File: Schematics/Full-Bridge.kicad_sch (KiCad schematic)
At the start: 0 parts

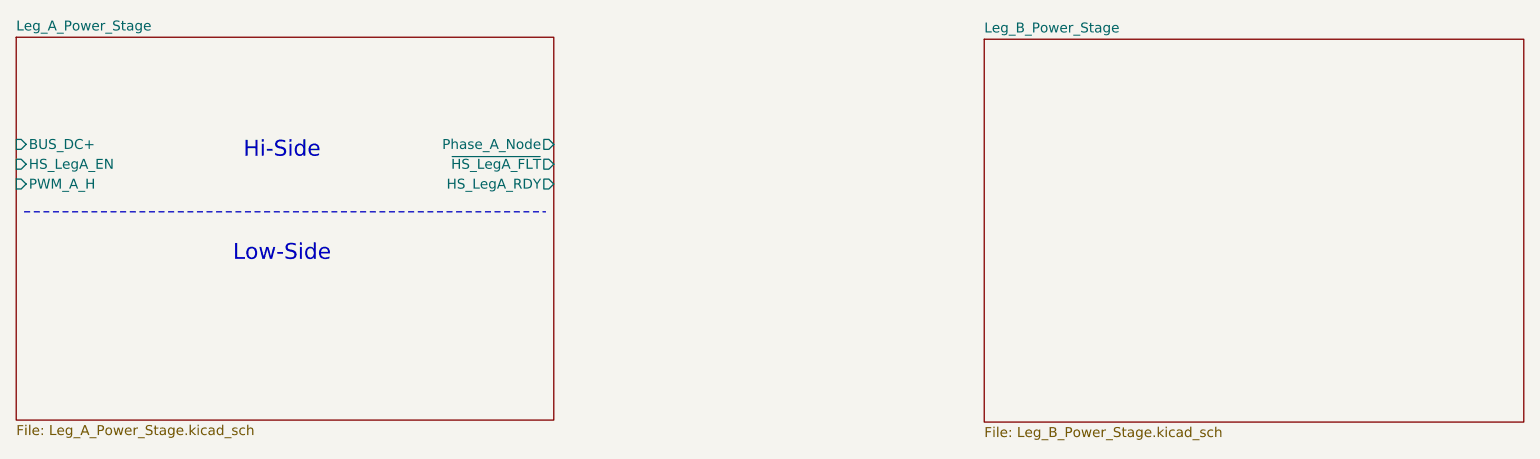
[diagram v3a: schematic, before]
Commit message: Adding 100 pf caps to Leg A circuit, WIP texts
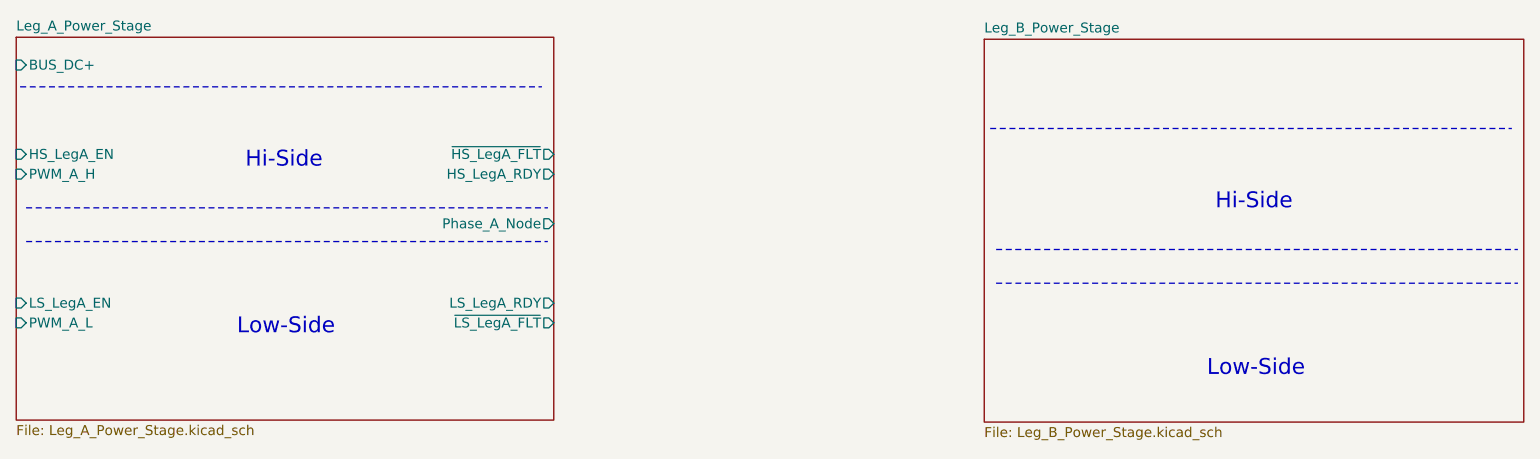
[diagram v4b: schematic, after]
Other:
- sheet Leg_A_Power_Stage ports: added LS_LegA_EN, LS_LegA_RDY, PWM_A_L, ~{LS_LegA_FLT}; removed none
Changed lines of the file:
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@@
 	(generator_version "9.0")
 	(paper "A4")
+	(text "Hi-Side\n"
+		(exclude_from_sim no)
+		(at 214.122 98.806 0)
+		(effects
+			(font
+				(size 2.032 2.032)
+			)
+		)
+	)
 	(text "Low-Side\n"
 		(exclude_from_sim no)
-		(at 89.662 105.41 0)
+		(at 90.17 114.808 0)
+		(effects
+			(font
+				(size 2.032 2.032)
+			)
+		)
+	)
+	(text "Low-Side\n"
+		(exclude_from_sim no)
+		(at 214.376 120.142 0)
 		(effects
 			(font
@@
 	(text "Hi-Side\n"
 		(exclude_from_sim no)
-		(at 89.662 92.202 0)
-		(effects
-			(font
-				(size 2.032 2.032)
-			)
-		)
-	)
-	(polyline
-		(pts
-			(xy 56.642 100.076) (xy 123.444 100.076)
+		(at 89.916 93.472 0)
+		(effects
+			(font
+				(size 2.032 2.032)
+			)
+		)
+	)
+	(polyline
+		(pts
+			(xy 181.102 104.902) (xy 247.904 104.902)
+		)
+		(stroke
+			(width 0)
+			(type dash)
+		)
+	)
+	(polyline
+		(pts
+			(xy 180.34 89.408) (xy 247.142 89.408)
+		)
+		(stroke
+			(width 0)
+			(type dash)
+		)
+	)
+	(polyline
+		(pts
+			(xy 56.896 103.886) (xy 123.698 103.886)
+		)
+		(stroke
+			(width 0)
+			(type dash)
+		)
+	)
+	(polyline
+		(pts
+			(xy 56.896 99.568) (xy 123.698 99.568)
+		)
+		(stroke
+			(width 0)
+			(type dash)
+		)
+	)
+	(polyline
+		(pts
+			(xy 56.134 84.074) (xy 122.936 84.074)
+		)
+		(stroke
+			(width 0)
+			(type dash)
+		)
+	)
+	(polyline
+		(pts
+			(xy 181.102 109.22) (xy 247.904 109.22)
 		)
 		(stroke
@@
 		)
 		(pin "BUS_DC+" input
-			(at 55.626 91.44 180)
+			(at 55.626 81.28 180)
 			(effects
 				(font
@@
 		)
 		(pin "HS_LegA_EN" input
-			(at 55.626 93.98 180)
+			(at 55.626 92.71 180)
 			(effects
 				(font
@@
 		)
 		(pin "HS_LegA_RDY" output
-			(at 124.46 96.52 0)
+			(at 124.46 95.25 0)
 			(effects
 				(font
@@
 		)
 		(pin "Phase_A_Node" output
-			(at 124.46 91.44 0)
+			(at 124.46 101.6 0)
 			(effects
 				(font
@@
 		)
 		(pin "PWM_A_H" input
-			(at 55.626 96.52 180)
+			(at 55.626 95.25 180)
 			(effects
 				(font
@@
 		)
 		(pin "~{HS_LegA_FLT}" output
-			(at 124.46 93.98 0)
-			(effects
-				(font
+			(at 124.46 92.71 0)
+			(effects
+				(font
+					(size 1.27 1.27)
+				)
+				(justify right)
+			)
+		)
+		(pin "LS_LegA_EN" input
+			(at 55.626 111.76 180)
+			(effects
+				(font
+					(size 1.27 1.27)
+				)
+				(justify left)
+			)
+		)
+		(pin "LS_LegA_RDY" output
+			(at 124.46 111.76 0)
+			(effects
+				(font
+					(size 1.27 1.27)
+				)
+				(justify right)
+			)
+		)
+		(pin "PWM_A_L" input
+			(at 55.626 114.3 180)
+			(effects
+				(font
+					(size 1.27 1.27)
+				)
+				(justify left)
+			)
+		)
+		(pin "~{LS_LegA_FLT}" output
+			(at 124.46 114.3 0)
+			(effects
+				(font

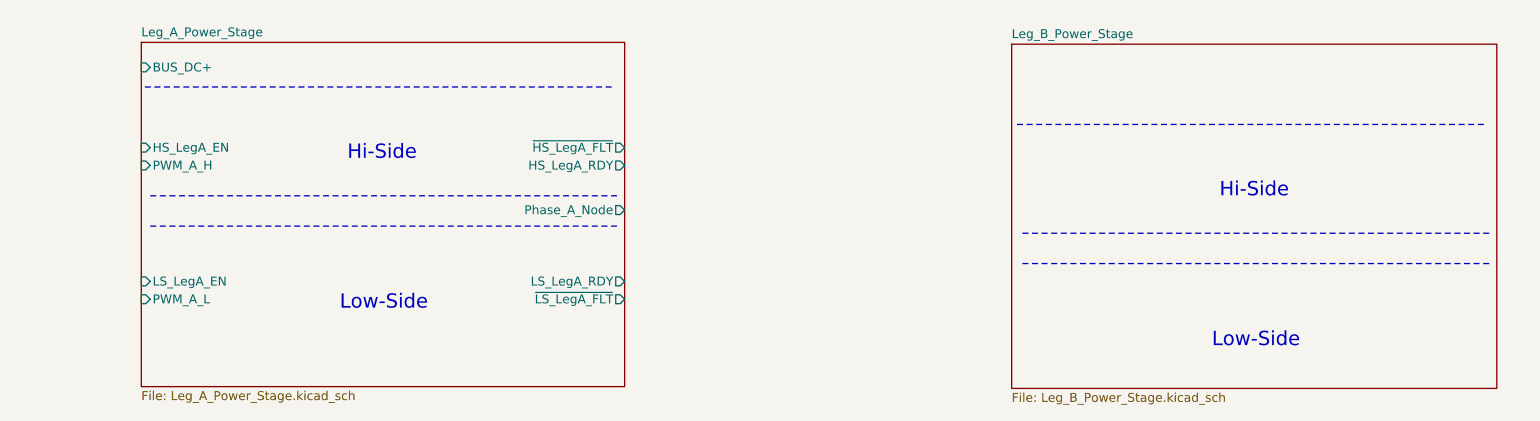
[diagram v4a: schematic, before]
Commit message: [WIP Full Bridge]
- Finished Leg B and cleaned up sub sheets Leg A and Leg B
- Added Hierarchical sheet pins for Leg A,B and Full Bridge
- Added power schamtic for future use
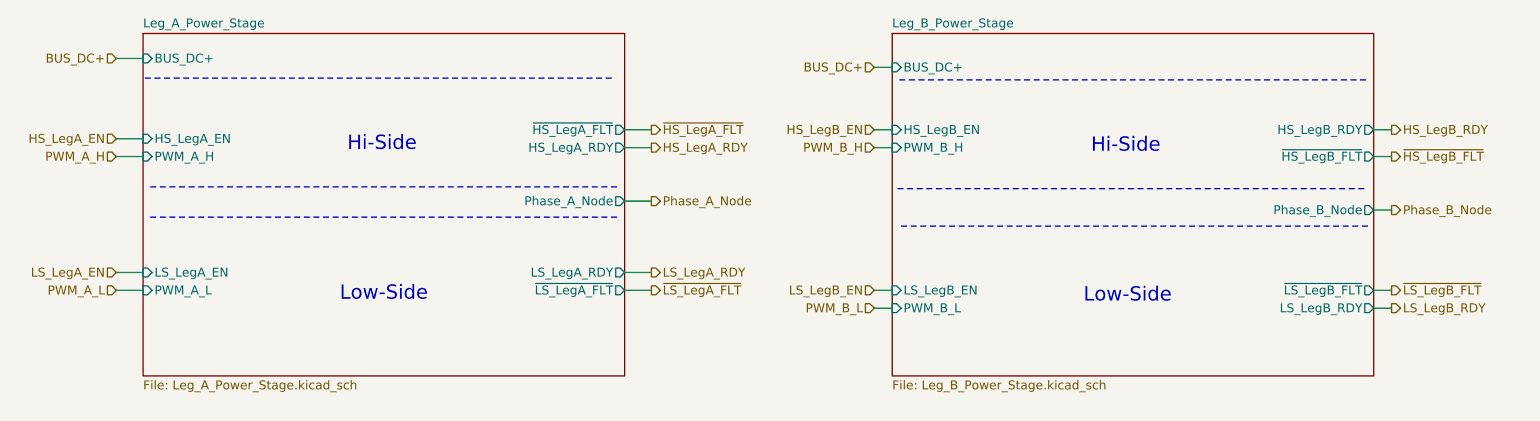
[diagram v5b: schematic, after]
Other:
- sheet Leg_B_Power_Stage ports: added BUS_DC+, HS_LegB_EN, HS_LegB_RDY, LS_LegB_EN, LS_LegB_RDY, PWM_B_H, PWM_B_L, Phase_B_Node, ~{HS_LegB_FLT}, ~{LS_LegB_FLT}; removed none

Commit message: Changing Text to Text Block
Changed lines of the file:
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@@
+		)
+	)
+	(text_box "Leg_B_Power_Stage"
+		(exclude_from_sim no)
+		(at 162.56 73.152 0)
+		(size 20.32 3.048)
+		(margins 0.9525 0.9525 0.9525 0.9525)
+		(stroke
+			(width 0)
+			(type solid)
+		)
+		(fill
+			(type color)
+			(color 0 0 255 0.1)
+		)
+		(effects
+			(font
+				(size 1.27 1.27)
+			)
+			(justify left top)
+		)
+	)
+	(text_box "Leg_A_Power_Stage"
+		(exclude_from_sim no)
+		(at 55.88 73.152 0)
+		(size 20.32 3.048)
+		(margins 0.9525 0.9525 0.9525 0.9525)
+		(stroke
+			(width 0)
+			(type solid)
+		)
+		(fill
+			(type color)
+			(color 0 0 255 0.1)
+		)
+		(effects
+			(font
+				(size 1.27 1.27)
+			)
+			(justify left top)
 		)
 	)
@@
 				)
 				(justify left bottom)
+				(hide yes)
 			)
 		)
@@
 				)
 				(justify left bottom)
-			)
-		)
+				(hide yes)
+			)
+		)

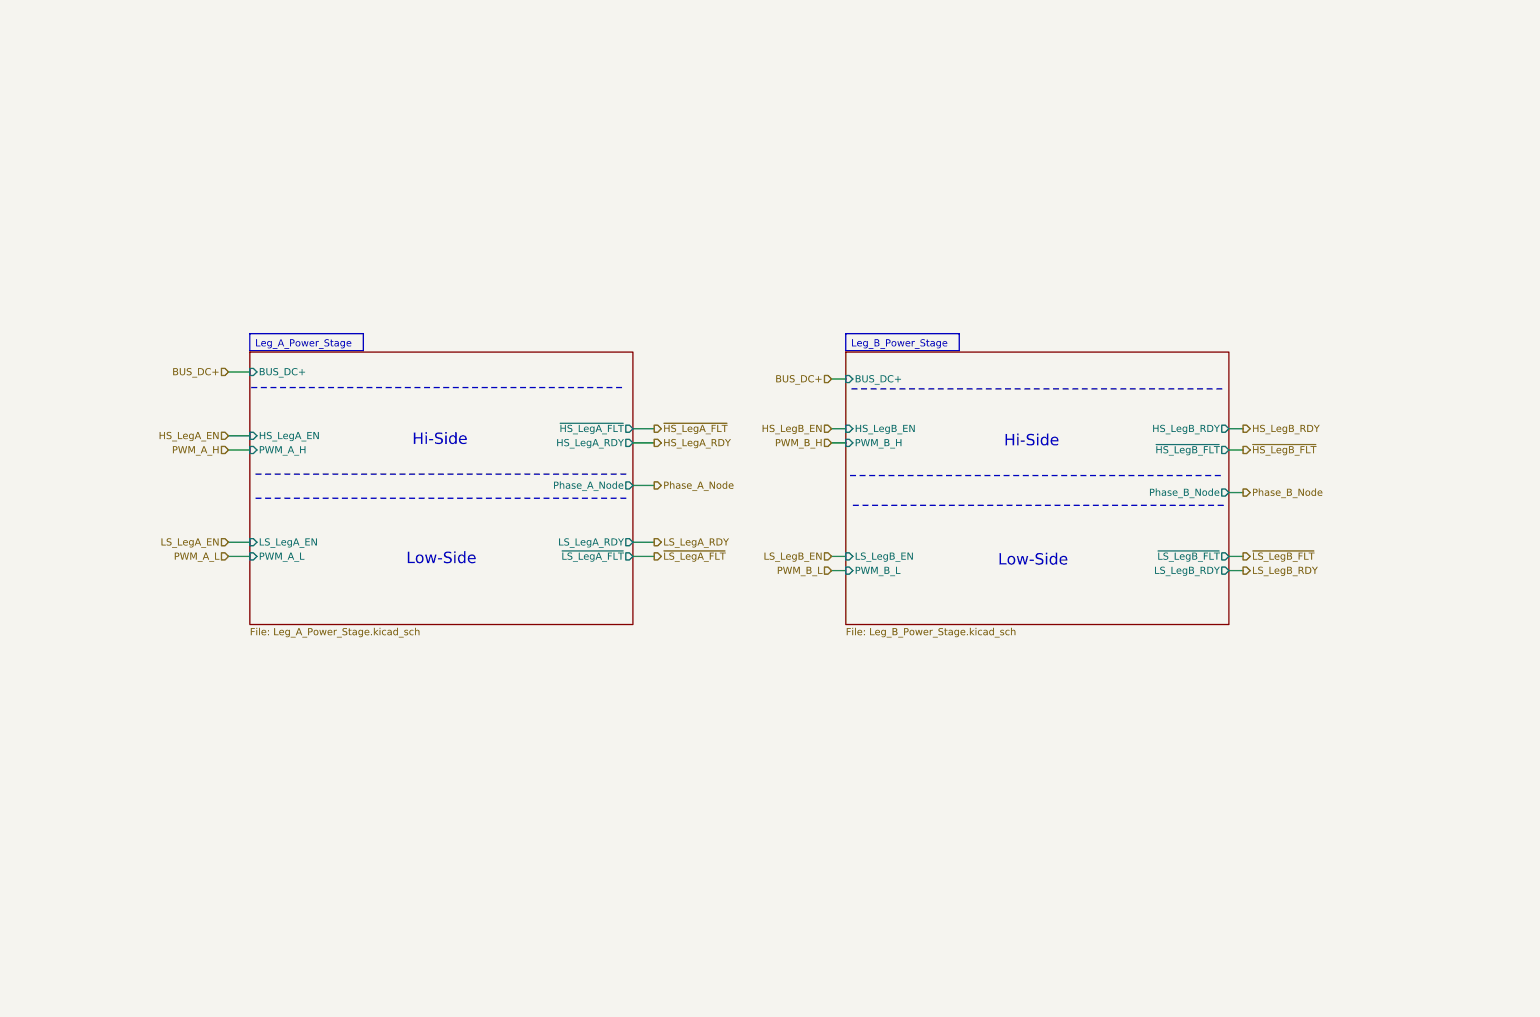
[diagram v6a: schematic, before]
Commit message: [WIP Single Phase SiC Inverter]
- Added molex 4 pin pcb connector for +15V power
- Added 3d model, symbol and footprint
- Added datasheet for molex connector
- Added Male and Female pcb - pcb connectors to all sub sheets
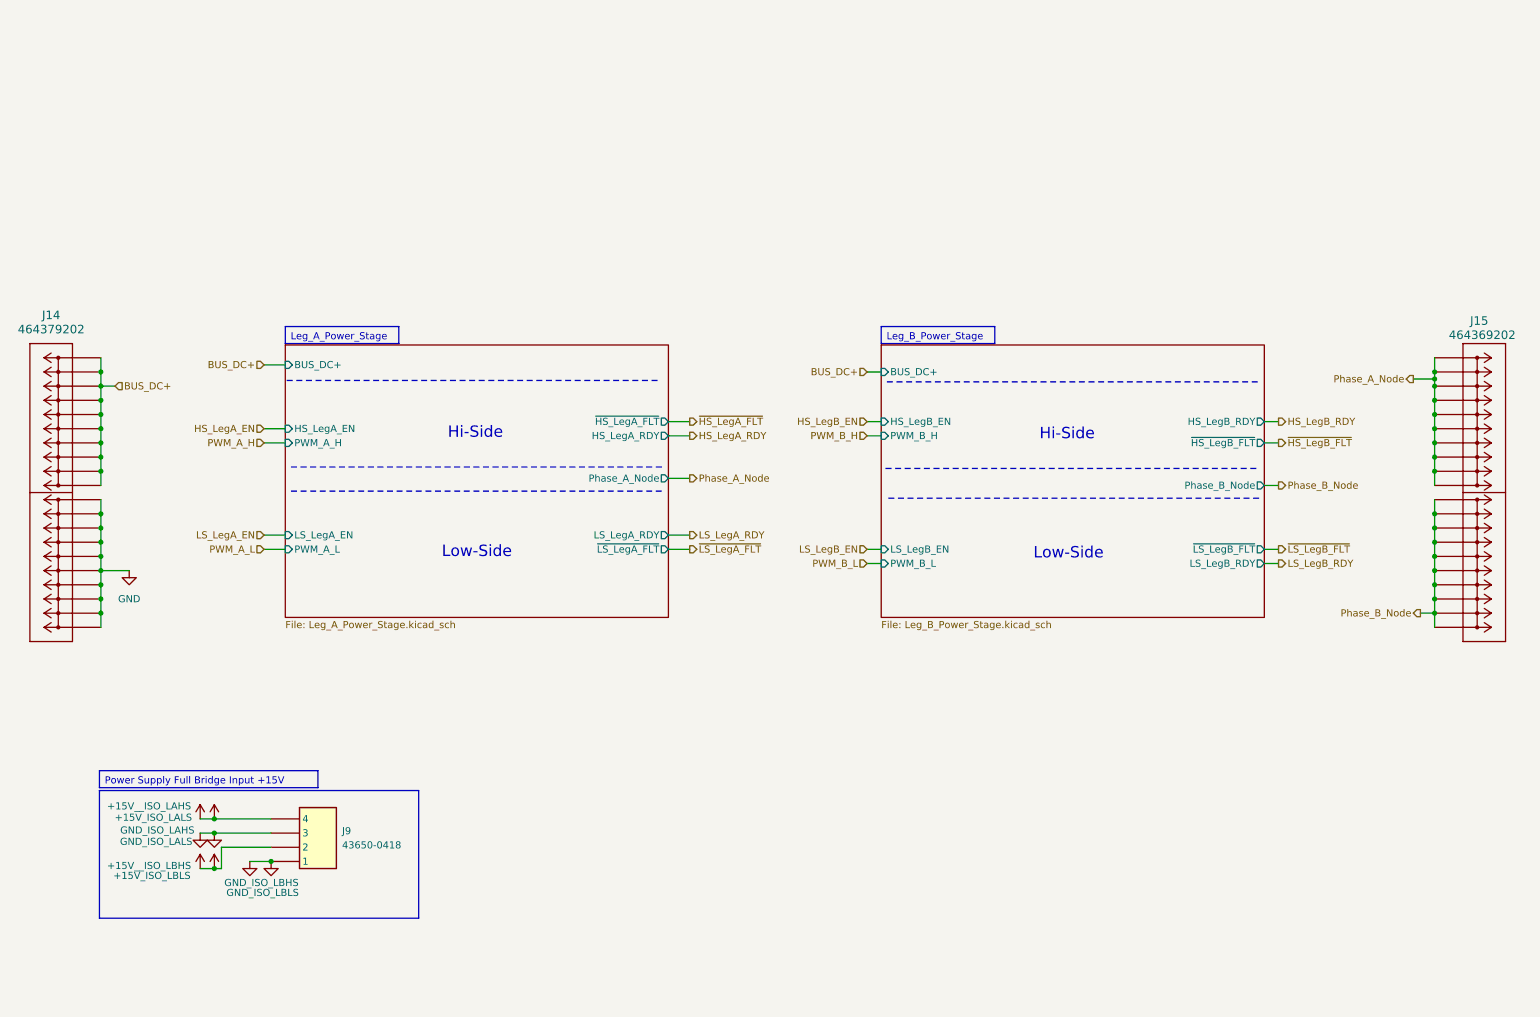
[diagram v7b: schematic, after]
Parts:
- added J14: 464379202, SiC_Inverter:46437-900_02, symbol SiC_Inverter:464379202
- added J15: 464369202, SiC_Inverter:46436-900_02, symbol SiC_Inverter:464369202
- added J9: 43650-0418, SiC_Inverter:436500418, symbol SiC_Inverter:43650-0418
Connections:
- net BUS_DC+: now also J14.P2_1, J14.P2_10, J14.P2_2, J14.P2_3, J14.P2_4, J14.P2_5, J14.P2_6, J14.P2_7, J14.P2_8, J14.P2_9
- net Phase_A_Node: now also J15.P1_1, J15.P1_10, J15.P1_2, J15.P1_3, J15.P1_4, J15.P1_5, J15.P1_6, J15.P1_7, J15.P1_8, J15.P1_9
- net Phase_B_Node: now also J15.P2_1, J15.P2_10, J15.P2_2, J15.P2_3, J15.P2_4, J15.P2_5, J15.P2_6, J15.P2_7, J15.P2_8, J15.P2_9
- new net +15V_ISO_LALS: J9.4
- new net +15V_ISO_LBLS: J9.2
- new net GND: J14.P1_1, J14.P1_10, J14.P1_2, J14.P1_3, J14.P1_4, J14.P1_5, J14.P1_6, J14.P1_7, J14.P1_8, J14.P1_9
- new net GND_ISO_LAHS: J9.3
- new net GND_ISO_LBHS: J9.1
